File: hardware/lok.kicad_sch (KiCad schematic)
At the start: 8 parts, among them J1 Conn_01x02_Pin, J2 Conn_01x02_Pin, U1 XIAO-ESP32-S3-SMD, U2 STSPIN233

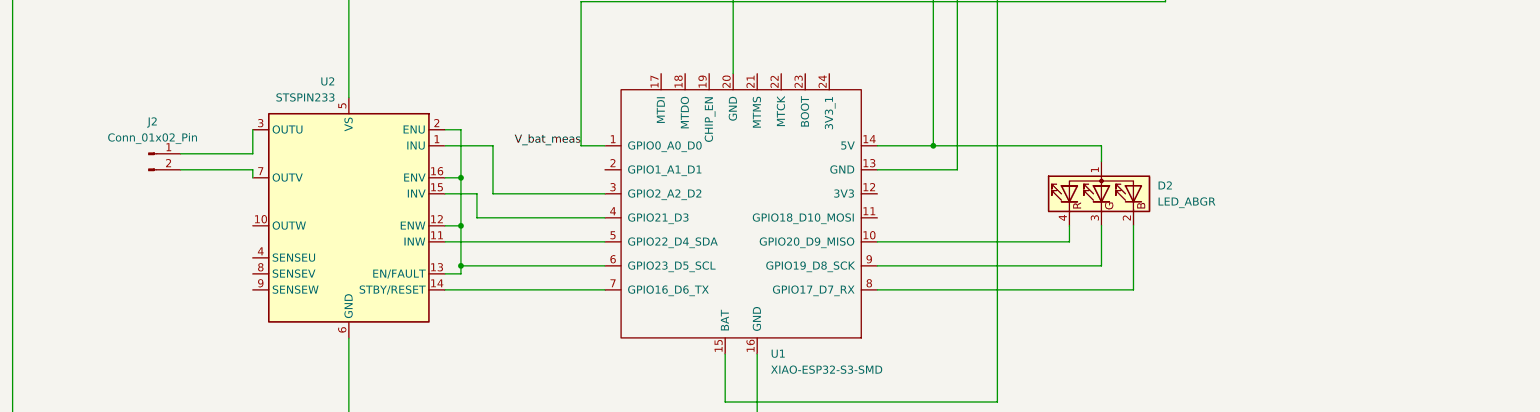
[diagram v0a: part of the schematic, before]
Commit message: added rgb leds
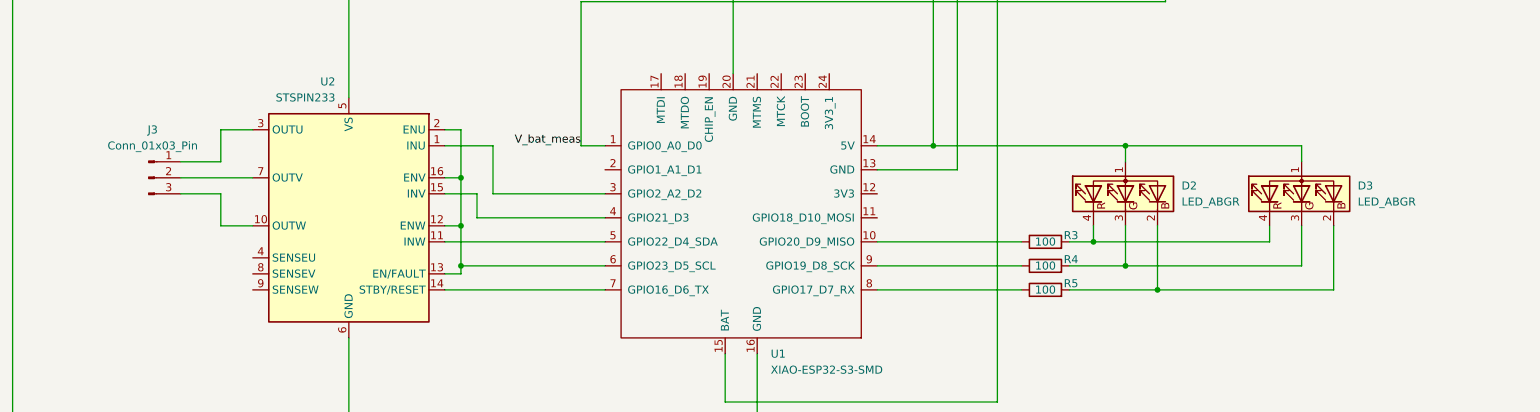
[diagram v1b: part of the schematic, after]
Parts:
- removed J2: Conn_01x02_Pin, Connector_PinHeader_2.54mm:PinHeader_1x02_P2.54mm_Vertical, symbol Connector:Conn_01x02_Pin
- added D3: LED_ABGR, symbol Device:LED_ABGR
- added J3: Conn_01x03_Pin, symbol Connector:Conn_01x03_Pin
- added R3, R4, R5: 100, Resistor_SMD:R_0603_1608Metric, symbol Device:R
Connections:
- net 5V: now also D3.1 (A)
- net at D2.2 (BK): now also D3.2 (BK), R5.2; no longer U1.8 (GPIO17_D7_RX)
- net at U1.9 (GPIO19_D8_SCK): now also R4.1; no longer D2.3 (GK)
- net at D2.4 (RK): now also D3.4 (RK), R3.2; no longer U1.10 (GPIO20_D9_MISO)
- net at U2.3 (OUTU): now also J3.1 (Pin_1)
- net at U2.7 (OUTV): now also J3.2 (Pin_2)
- net at U2.10 (OUTW): now also J3.3 (Pin_3)
- new net: D2.3 (GK), D3.3 (GK), R4.2
- new net: R3.1, U1.10 (GPIO20_D9_MISO)
- new net: R5.1, U1.8 (GPIO17_D7_RX)
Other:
- moved on the sheet: D2

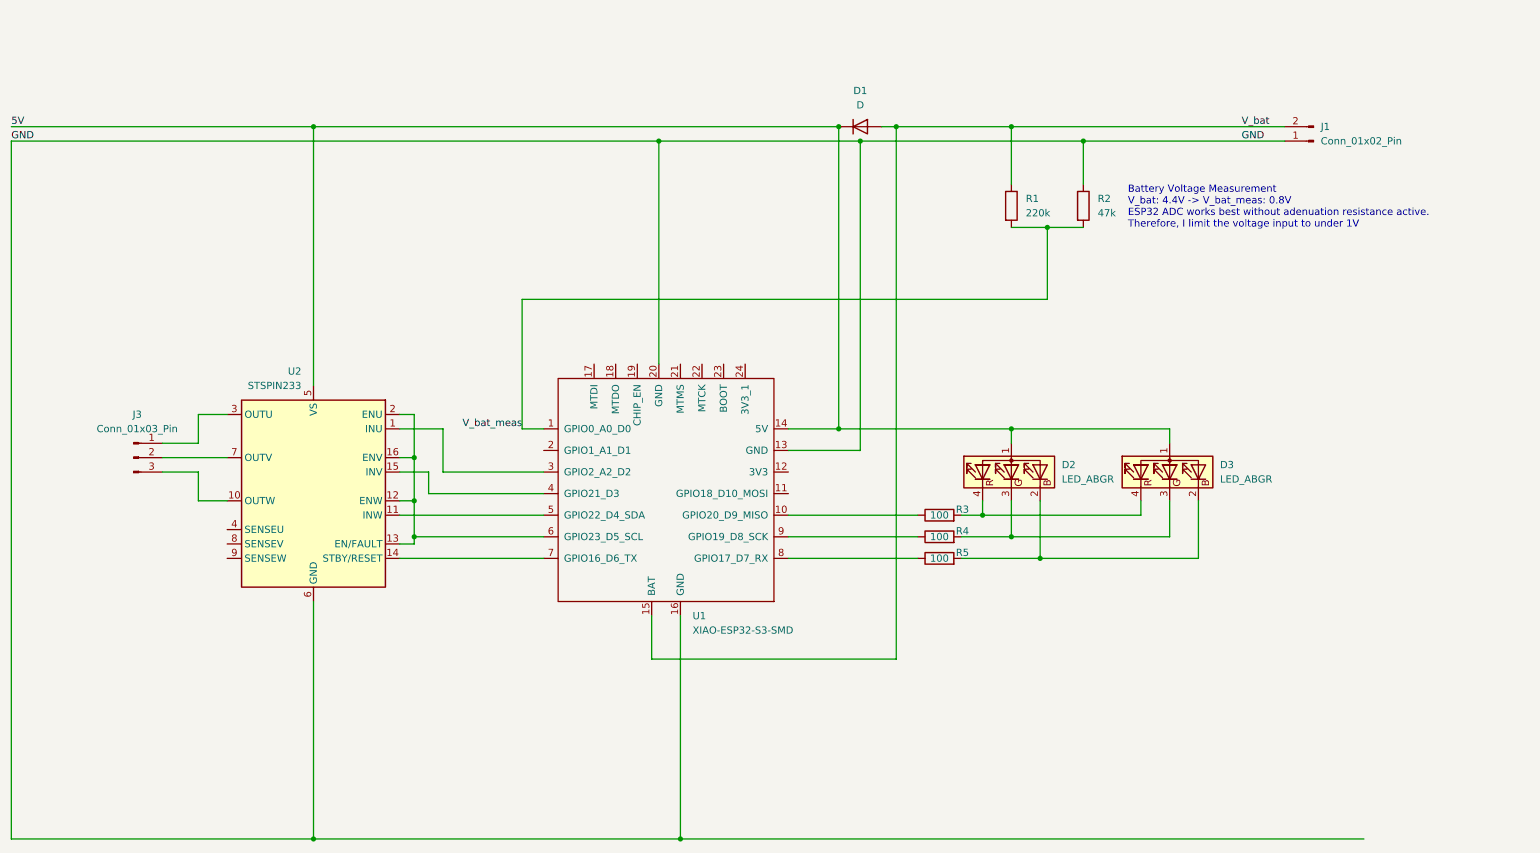
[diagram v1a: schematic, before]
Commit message: added battery holder
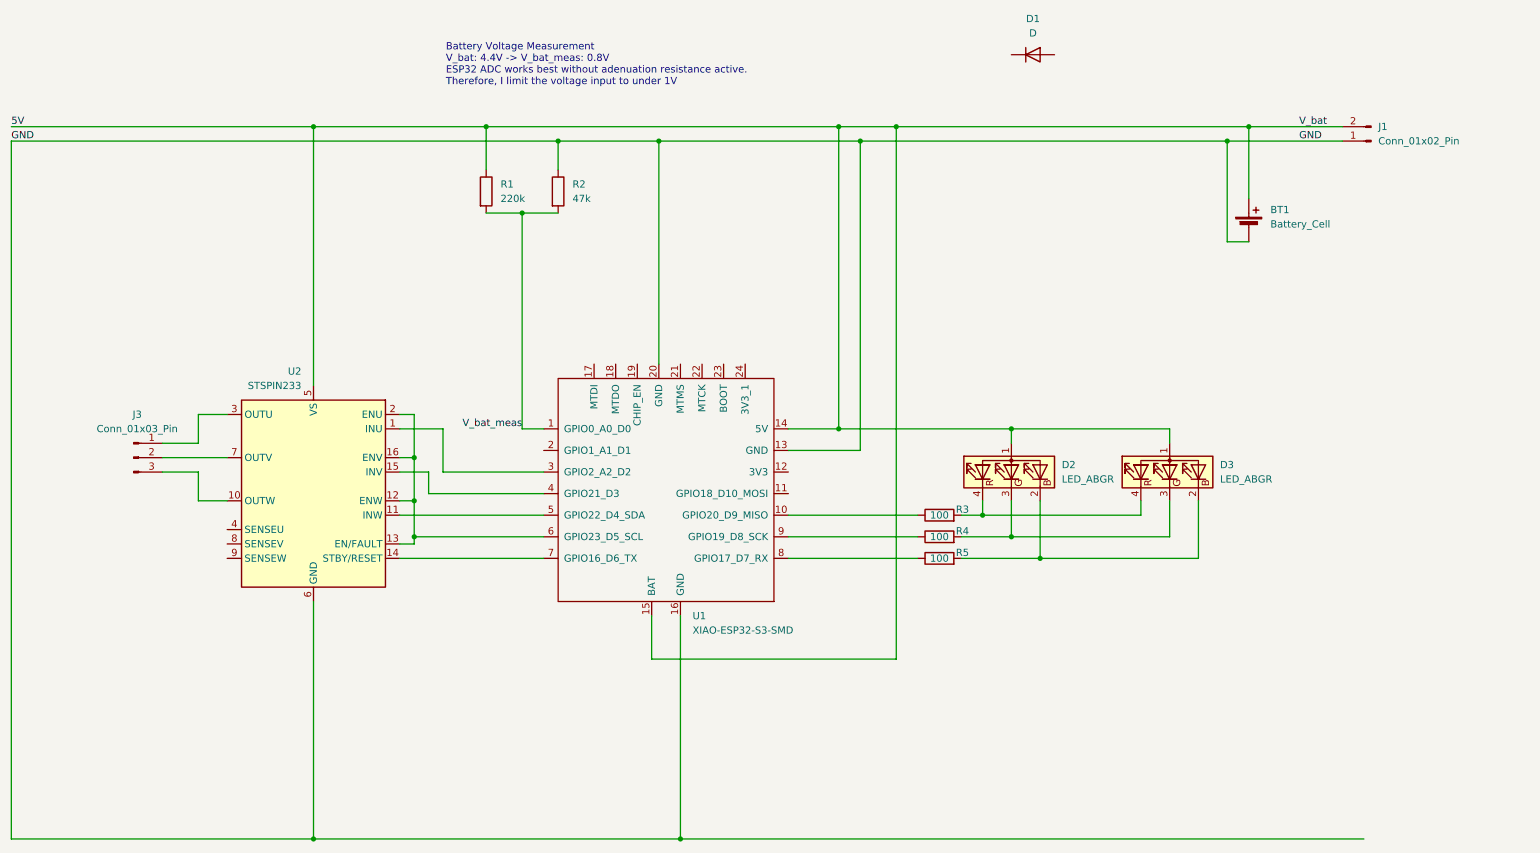
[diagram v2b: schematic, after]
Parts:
- added BT1: Battery_Cell, Battery:BatteryHolder_Keystone_1042_1x18650, symbol Device:Battery_Cell
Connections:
- net 5V: now also J1.2 (Pin_2), R1.1, U1.15 (BAT), BT1.1 (+); no longer D1.1 (K)
- net GND: now also BT1.2 (-)
- removed net V_bat: D1.2 (A), J1.2 (Pin_2), R1.1, U1.15 (BAT)
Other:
- moved on the sheet: D1, J1, R1, R2
